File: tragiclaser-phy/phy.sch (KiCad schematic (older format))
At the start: 26 parts, among them J2 BEL_FUSE_0826-1G1T-23-F, J3 BEL_FUSE_0826-1G1T-23-F, P1 CONN_01X10, P2 SMA, P3 SMA, U1 XC6SLX25-2FTG256C

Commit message: Began layout on TRAGICLASER PHY
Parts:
- removed J3: BEL_FUSE_0826-1G1T-23-F, symbol BEL_FUSE_0826-1G1T-23-F
- removed P1: CONN_01X10, symbol CONN_01X10
- removed P2, P3: SMA, symbol BNC
- removed R29: 100, symbol R
- removed R30, R31: 1k, symbol R
- removed R32: 0, symbol R
- added C? (x2): 0.47 uF, azonenberg_pcb:EIA_0402_CAP_NOSILK, symbol C
- added P1: CONN_01X12, azonenberg_pcb:CONN_HEADER_2.54MM_2x6_RA, symbol CONN_01X12
- added R33, R34, R37, R38: 953, azonenberg_pcb:EIA_0402_RES_NOSILK, symbol R
- added TP1, TP4, TP5, TP6: SMA, azonenberg_pcb:CONN_SMA_EDGE_SAMTEC_SMA_J_P_H_ST_EM1, symbol BNC
- added TP7, TP8: CONN_01X01, azonenberg_pcb:TESTPOINT_SMT_0.5MM, symbol CONN_01X01
- added TP9: CONN_01X01, azonenberg_pcb:TESTPOINT_SMT_KEYSTONE_5016, symbol CONN_01X01
- J2: footprint (none) -> azonenberg_pcb:CONN_BELFUSE_0826_1G1T_23_F
- R10, R11, R12, R13, R14, R15, R16, R17, R18, R3, R4, R5, R6, R7, R8, R9: footprint (none) -> azonenberg_pcb:EIA_0402_RES_NOSILK
- U1: footprint (none) -> azonenberg_pcb:BGA_256_17x17_FULLARRAY_1MM
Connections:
- net 3V3: now also P1.11 (P11)
- net GND: now also C?.1, C?.2, P1.12 (P12), TP1.2 (Ext), TP4.2 (Ext), TP5.2 (Ext), TP6.2 (Ext), TP9.1 (P1)
- net GPIO0: now also P1.1 (P1)
- net GPIO1: now also P1.2 (P2)
- net GPIO2: now also P1.3 (P3)
- net GPIO3: now also P1.4 (P4)
- net GPIO4: now also P1.5 (P5)
- net GPIO5: now also P1.6 (P6)
- net GPIO6: now also U1.C9 (IO_L34P_GCLK19_0), P1.7 (P7); no longer U1.D8 (IO_L38P_0)
- net GPIO7: now also U1.B6 (IO_L04P_0), P1.8 (P8); no longer U1.C8 (IO_L38N_VREF_0)
- net LED1_P: now also U1.C5 (IO_L03N_0); no longer U1.C11 (IO_L39P_0)
- net RX_N: now also R34.1
- net RX_P: now also U1.B8 (IO_L33P_0), U1.D8 (IO_L38P_0), R33.2; no longer U1.B10 (IO_L35P_GCLK17_0), U1.C9 (IO_L34P_GCLK19_0)
- net TX_N: now also J2.10 (CH1_N), R38.1; no longer J2.2 (CH3_N)
- net TX_N_A: now also U1.A5 (IO_L02N_0), U1.B5 (IO_L02P_0); no longer U1.A8 (IO_L33N_0), U1.B8 (IO_L33P_0)
- net TX_N_B: now also U1.A4 (IO_L01N_VREF_0); no longer U1.A5 (IO_L02N_0)
- net TX_P: now also J2.11 (CH1_P), R37.2; no longer J2.3 (CH3_P)
- net TX_P_A: now also U1.A10 (IO_L35N_GCLK16_0), U1.B10 (IO_L35P_GCLK17_0); no longer U1.A6 (IO_L04N_0), U1.B6 (IO_L04P_0)
- net TX_P_B: now also U1.A9 (IO_L34N_GCLK18_0); no longer U1.B5 (IO_L02P_0)
- net TX_TAP: now also J2.12 (CH1_TAP); no longer J2.1 (CH3_TAP)
- net VREF_1V5: now also U1.A8 (IO_L33N_0), C?.1, TP8.1 (P1); no longer U1.A10 (IO_L35N_GCLK16_0)
- net VREF_1V8: now also U1.C8 (IO_L38N_VREF_0), C?.2, TP7.1 (P1); no longer U1.A9 (IO_L34N_GCLK18_0)
- new net: R33.1, TP4.1 (In)
- new net: R34.2, TP5.1 (In)
- new net: R37.1, TP1.1 (In)
- new net: R38.2, TP6.1 (In)
- new net GPIO8: P1.9 (P9), U1.A6 (IO_L04N_0)
- new net GPIO9: P1.10 (P10), U1.C11 (IO_L39P_0)
- no-connect marks 34 -> 19
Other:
- note added: "Test points include built-in 20x transmission line probes\nConnect directly w/ SMA to 50 ohm scope input\n1K loading on DUT when active"
- note removed: "Second RJ45 for easy scope probing"
- note removed: "TODO: confirm correct pair\nassignments before layout"
- moved on the sheet: R10, R11, R4, R9

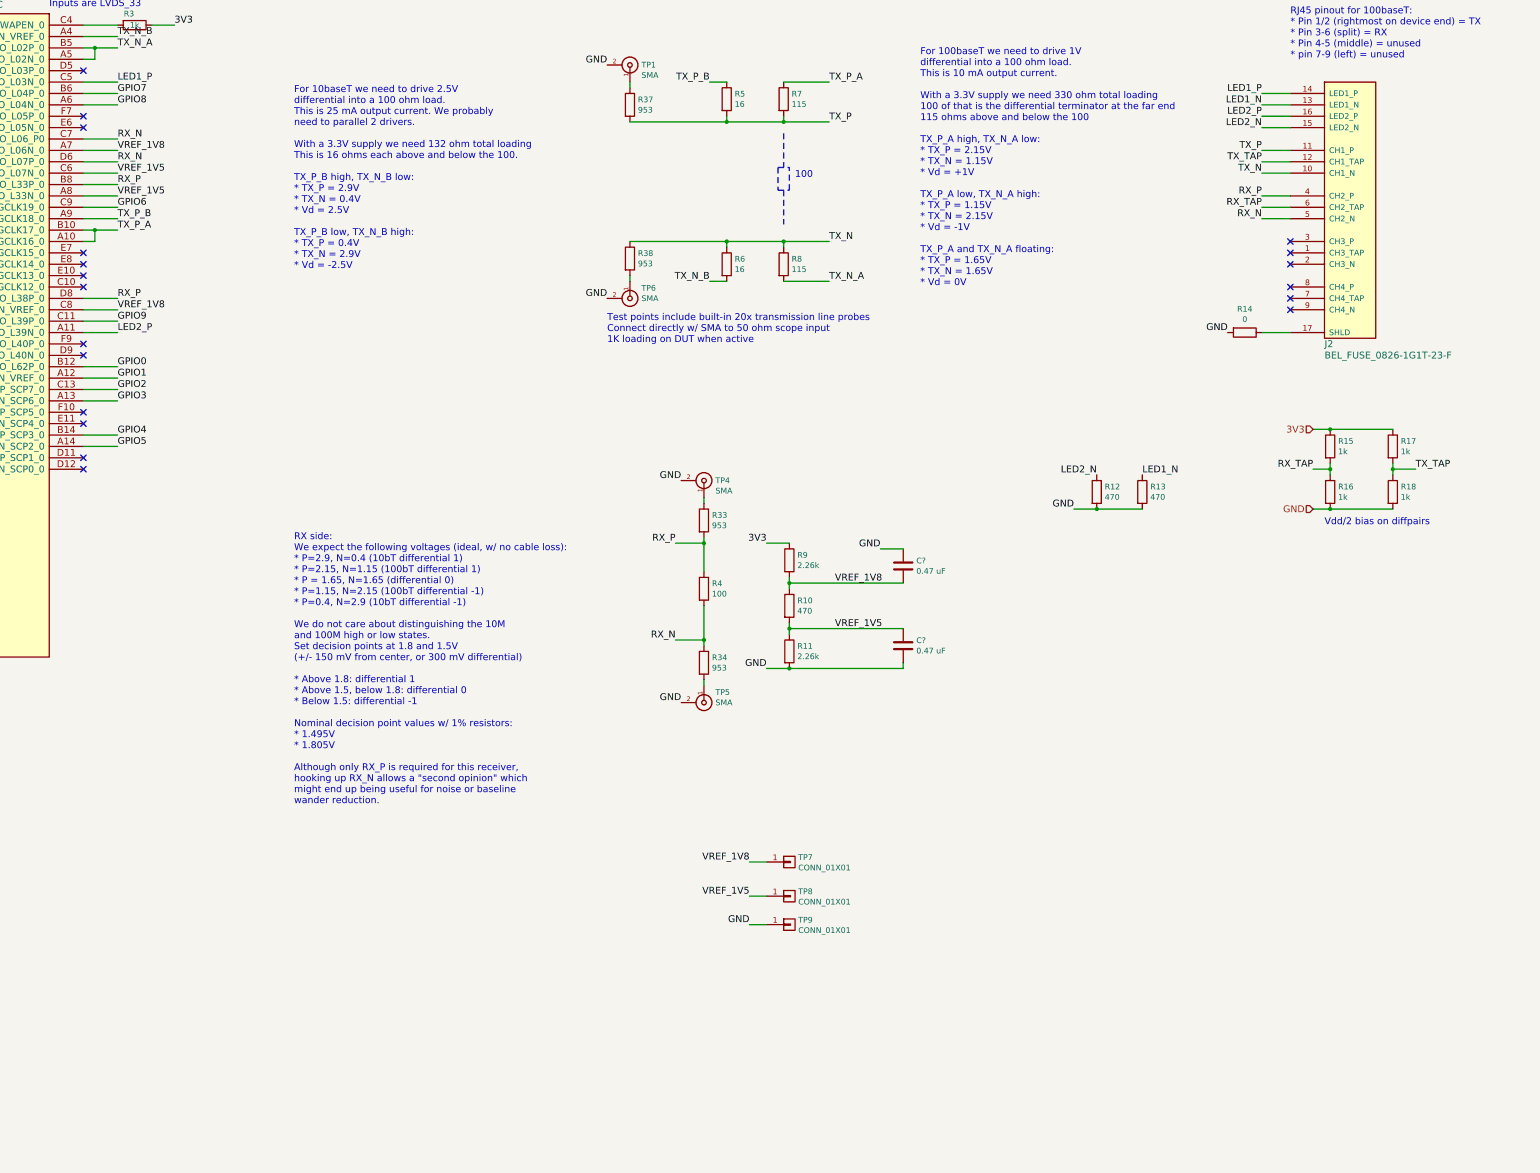
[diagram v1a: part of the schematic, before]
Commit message: Finished initial layout, ready for design review
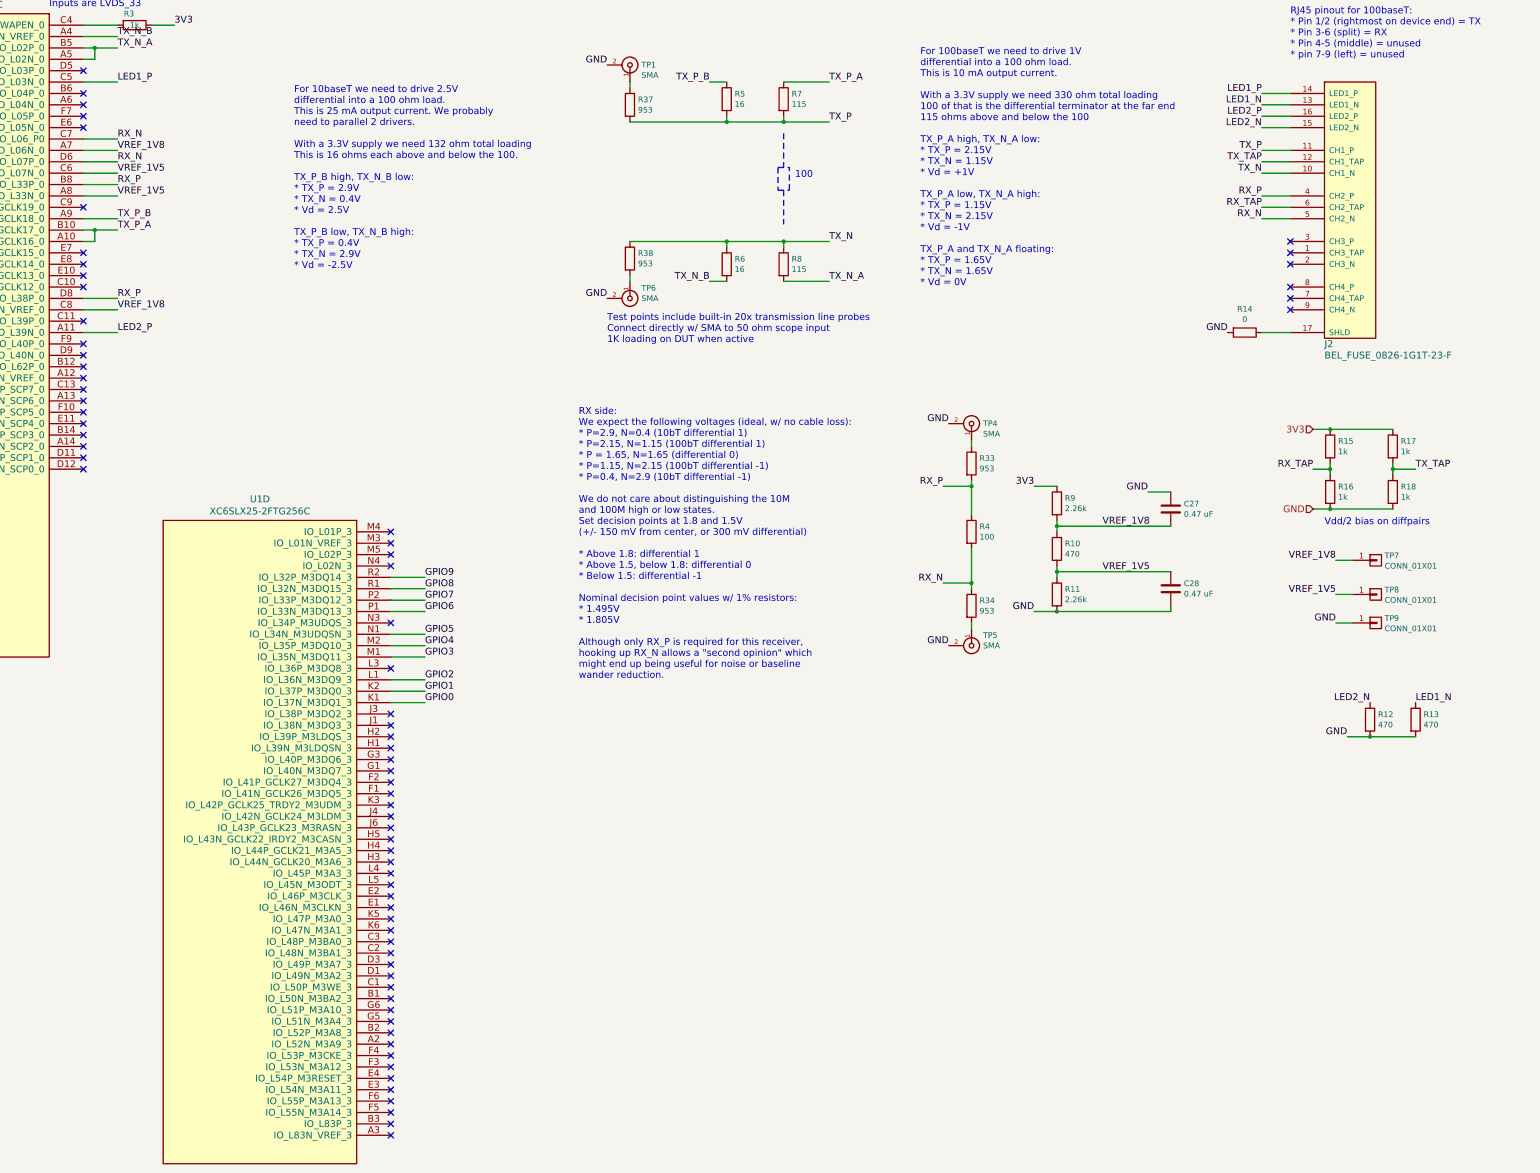
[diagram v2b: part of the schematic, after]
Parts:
- added unit 4 of U1
- gave numbers to parts that had none: 2
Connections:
- net GPIO0: now also U1.K1 (IO_L37N_M3DQ1_3); no longer U1.B12 (IO_L62P_0)
- net GPIO1: now also U1.K2 (IO_L37P_M3DQ0_3); no longer U1.A12 (IO_L62N_VREF_0)
- net GPIO2: now also U1.L1 (IO_L36N_M3DQ9_3); no longer U1.C13 (IO_L63P_SCP7_0)
- net GPIO3: now also U1.M1 (IO_L35N_M3DQ11_3); no longer U1.A13 (IO_L63N_SCP6_0)
- net GPIO4: now also U1.M2 (IO_L35P_M3DQ10_3); no longer U1.B14 (IO_L65P_SCP3_0)
- net GPIO5: now also U1.N1 (IO_L34N_M3UDQSN_3); no longer U1.A14 (IO_L65N_SCP2_0)
- net GPIO6: now also U1.P1 (IO_L33N_M3DQ13_3); no longer U1.C9 (IO_L34P_GCLK19_0)
- net GPIO7: now also U1.P2 (IO_L33P_M3DQ12_3); no longer U1.B6 (IO_L04P_0)
- net GPIO8: now also U1.R1 (IO_L32N_M3DQ15_3); no longer U1.A6 (IO_L04N_0)
- net GPIO9: now also U1.R2 (IO_L32P_M3DQ14_3); no longer U1.C11 (IO_L39P_0)
- no-connect marks 19 -> 73
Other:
- moved on the sheet: C27, C28, R10, R11, R12, R13, R33, R34, R4, R9, TP4, TP5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

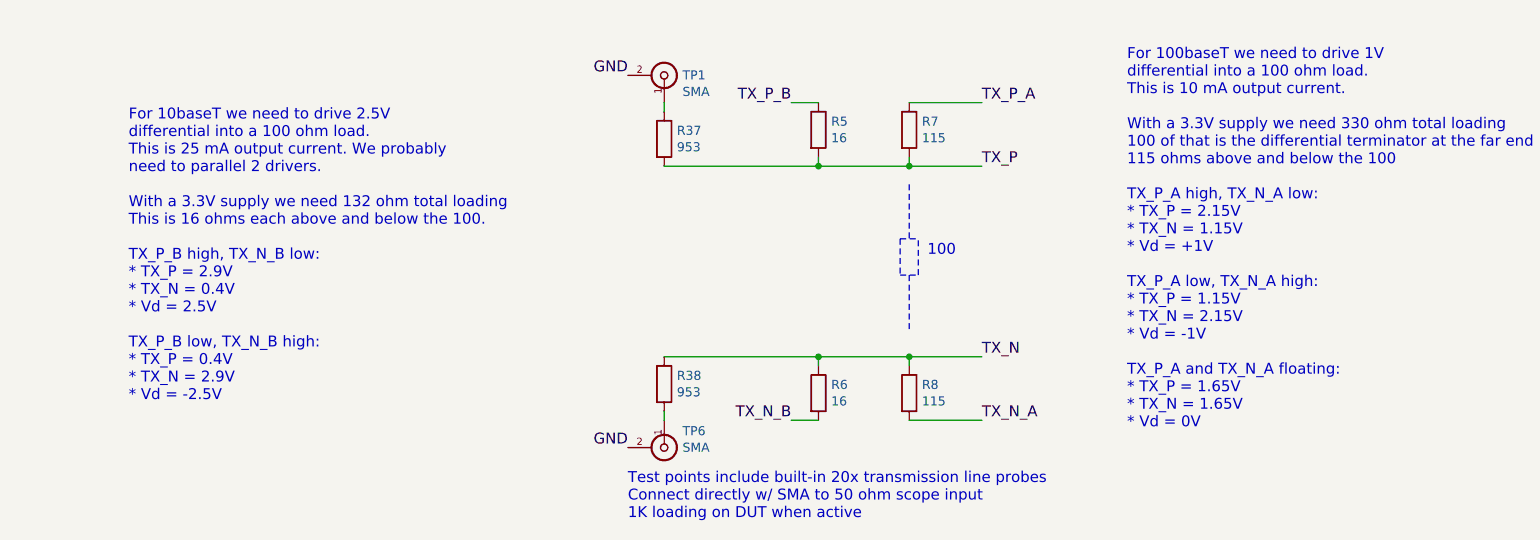
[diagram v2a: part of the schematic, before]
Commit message: PHY: fixed swapped resistor values
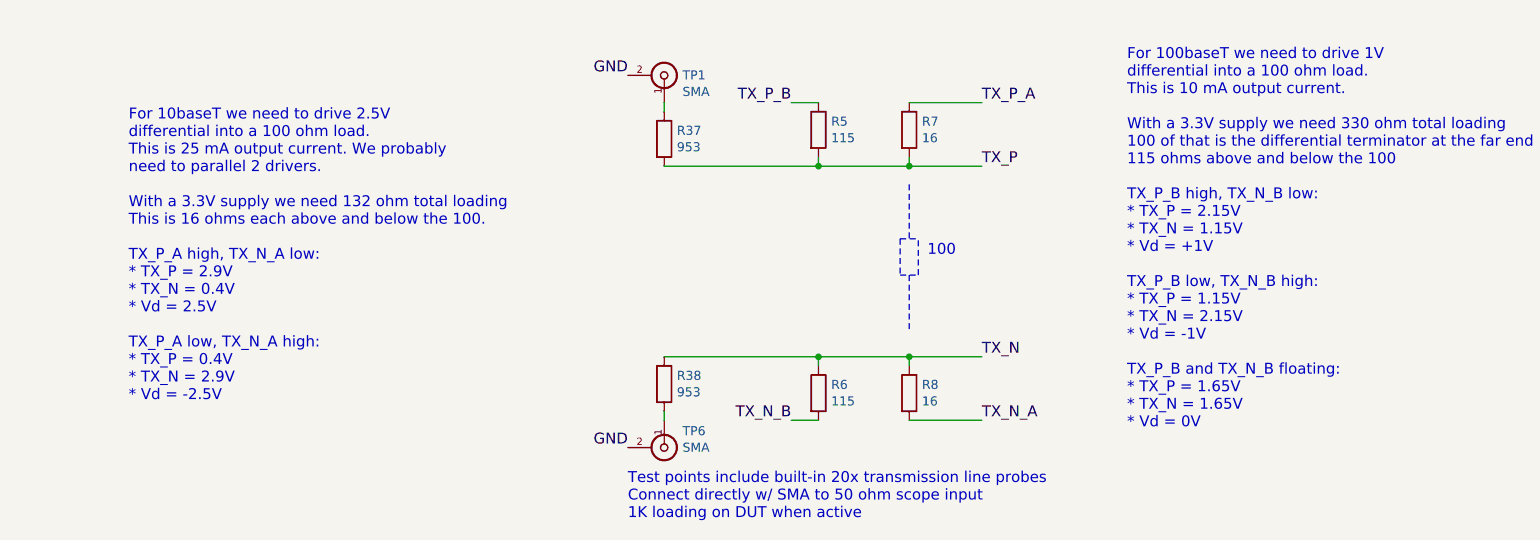
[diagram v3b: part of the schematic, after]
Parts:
- R5, R6: value 16 -> 115
- R7, R8: value 115 -> 16
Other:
- note added: "For 100baseT we need to drive 1V\ndifferential into a 100 ohm load.\nThis is 10 mA output current.\n\nWith a 3.3V supply we need 330 ohm total loading\n100 of that is the differential terminator at the far end\n115 ohms above and below the 100\n\nTX_P_B high, TX_N_B low:\n* TX_P = 2.15V\n* TX_N = 1.15V\n* Vd = +1V\n\nTX_P_B low, TX_N_B high:\n* TX_P = 1.15V\n* TX_N = 2.15V\n* Vd = -1V\n\nTX_P_B a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"
- note added: "For 10baseT we need to drive 2.5V\ndifferential into a 100 ohm load.\nThis is 25 mA output current. We probably\nneed to parallel 2 drivers.\n\nWith a 3.3V supply we need 132 ohm total loading\nThis is 16 ohms each above and below the 100.\n\nTX_P_A high, TX_N_A low:\n* TX_P = 2.9V\n* TX_N = 0.4V\n* Vd = 2.5V\n\nTX_P_A low, TX_N_A high:\n* TX_P = 0.4V\n* TX_N = 2.9V\n* Vd = -2.5V"
- note removed: "For 100baseT we need to drive 1V\ndifferential into a 100 ohm load.\nThis is 10 mA output current.\n\nWith a 3.3V supply we need 330 ohm total loading\n100 of that is the differential terminator at the far end\n115 ohms above and below the 100\n\nTX_P_A high, TX_N_A low:\n* TX_P = 2.15V\n* TX_N = 1.15V\n* Vd = +1V\n\nTX_P_A low, TX_N_A high:\n* TX_P = 1.15V\n* TX_N = 2.15V\n* Vd = -1V\n\nTX_P_A a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"
- note removed: "For 10baseT we need to drive 2.5V\ndifferential into a 100 ohm load.\nThis is 25 mA output current. We probably\nneed to parallel 2 drivers.\n\nWith a 3.3V supply we need 132 ohm total loading\nThis is 16 ohms each above and below the 100.\n\nTX_P_B high, TX_N_B low:\n* TX_P = 2.9V\n* TX_N = 0.4V\n* Vd = 2.5V\n\nTX_P_B low, TX_N_B high:\n* TX_P = 0.4V\n* TX_N = 2.9V\n* Vd = -2.5V"
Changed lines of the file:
@@
 P 9000 1550
 F 0 "R7" H 9070 1596 50  0000 L CNN
-F 1 "115" H 9070 1505 50  0000 L CNN
+F 1 "16" H 9070 1505 50  0000 L CNN
 F 2 "azonenberg_pcb:EIA_0402_RES_NOSILK" V 8930 1550 50  0001 C CNN
 F 3 "" H 9000 1550 50  0000 C CNN
@@
 P 9000 3000
 F 0 "R8" H 9070 3046 50  0000 L CNN
-F 1 "115" H 9070 2955 50  0000 L CNN
+F 1 "16" H 9070 2955 50  0000 L CNN
 F 2 "azonenberg_pcb:EIA_0402_RES_NOSILK" V 8930 3000 50  0001 C CNN
 F 3 "" H 9000 3000 50  0000 C CNN
@@
 TX_N_A
 Text Notes 4700 3050 0    60   ~ 0
-For 10baseT we need to drive 2.5V\ndifferential into a 100 ohm load.\nThis is 25 mA output current. We probably\nneed to parallel 2 drivers.\n\nWith a 3.3V supply we need 132 ohm total loading\nThis is 16 ohms each above and below the 100.\n\nTX_P_B high, TX_N_B low:\n* TX_P = 2.9V\n* TX_N = 0.4V\n* Vd = 2.5V\n\nTX_P_B low, TX_N_B high:\n* TX_P = 0.4V\n* TX_N = 2.9V\n* Vd = -2.5V
+For 10baseT we need to drive 2.5V\ndifferential into a 100 ohm load.\nThis is 25 mA output current. We probably\nneed to parallel 2 drivers.\n\nWith a 3.3V supply we need 132 ohm total loading\nThis is 16 ohms each above and below the 100.\n\nTX_P_A high, TX_N_A low:\n* TX_P = 2.9V\n* TX_N = 0.4V\n* Vd = 2.5V\n\nTX_P_A low, TX_N_A high:\n* TX_P = 0.4V\n* TX_N = 2.9V\n* Vd = -2.5V
 Text Notes 10200 3200 0    60   ~ 0
-For 100baseT we need to drive 1V\ndifferential into a 100 ohm load.\nThis is 10 mA output current.\n\nWith a 3.3V supply we need 330 ohm total loading\n100 of that is the differential terminator at the far end\n115 ohms above and below the 100\n\nTX_P_A high, TX_N_A low:\n* TX_P = 2.15V\n* TX_N = 1.15V\n* Vd = +1V\n\nTX_P_A low, TX_N_A high:\n* TX_P = 1.15V\n* TX_N = 2.15V\n* Vd = -1V\n\nTX_P_A and TX_N_A floating:\n* TX_P = 1.65V\n* TX_N = 1.65V\n* Vd = 0V
+For 100baseT we need to drive 1V\ndifferential into a 100 ohm load.\nThis is 10 mA output current.\n\nWith a 3.3V supply we need 330 ohm total loading\n100 of that is the differential terminator at the far end\n115 ohms above and below the 100\n\nTX_P_B high, TX_N_B low:\n* TX_P = 2.15V\n* TX_N = 1.15V\n* Vd = +1V\n\nTX_P_B low, TX_N_B high:\n* TX_P = 1.15V\n* TX_N = 2.15V\n* Vd = -1V\n\nTX_P_B and TX_N_B floating:\n* TX_P = 1.65V\n* TX_N = 1.65V\n* Vd = 0V
 Text Notes 9100 2250 0    60   ~ 0
 100
@@
 P 8500 1550
 F 0 "R5" H 8570 1596 50  0000 L CNN
-F 1 "16" H 8570 1505 50  0000 L CNN
+F 1 "115" H 8570 1505 50  0000 L CNN
 F 2 "azonenberg_pcb:EIA_0402_RES_NOSILK" V 8430 1550 50  0001 C CNN
 F 3 "" H 8500 1550 50  0000 C CNN
@@
 P 8500 3000
 F 0 "R6" H 8570 3046 50  0000 L CNN
-F 1 "16" H 8570 2955 50  0000 L CNN
+F 1 "115" H 8570 2955 50  0000 L CNN
 F 2 "azonenberg_pcb:EIA_0402_RES_NOSILK" V 8430 3000 50  0001 C CNN
 F 3 "" H 8500 3000 50  0000 C CNN
